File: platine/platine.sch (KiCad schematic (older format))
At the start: 16 parts

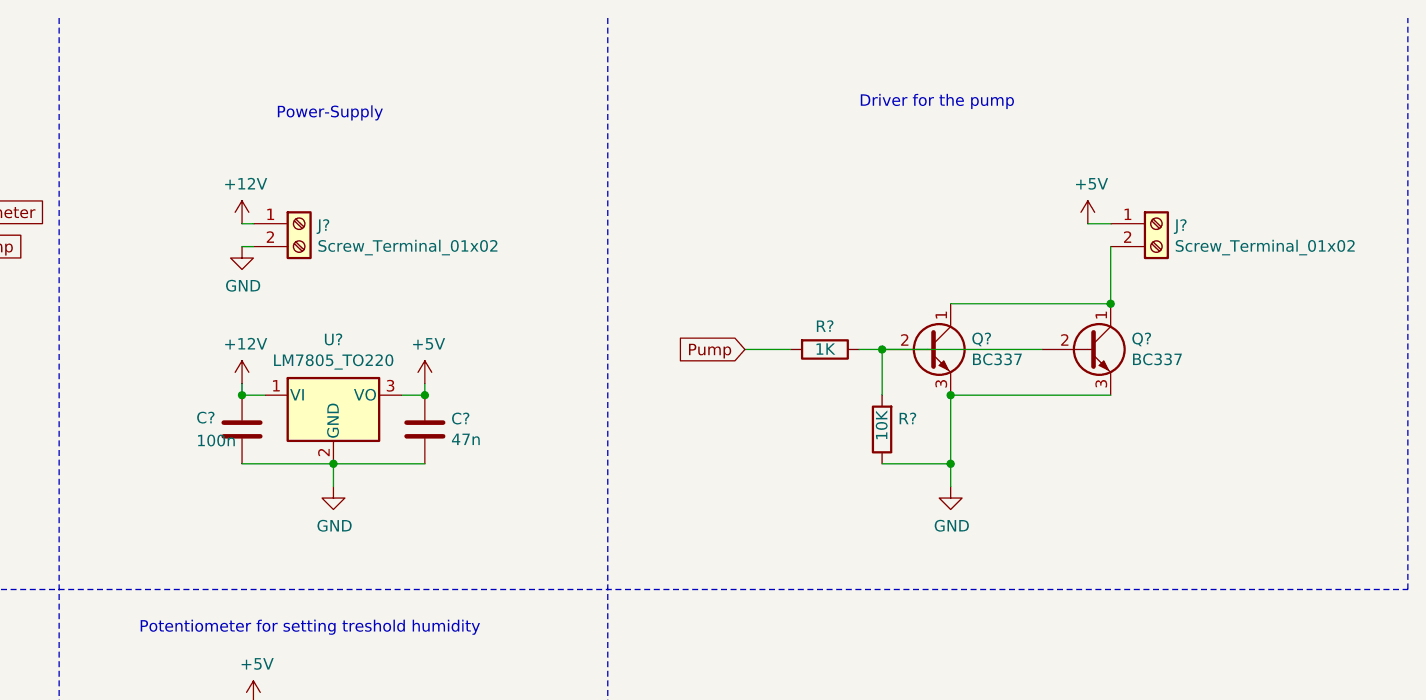
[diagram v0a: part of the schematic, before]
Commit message: Firmware timer-based and removed unnecessaries from scematics
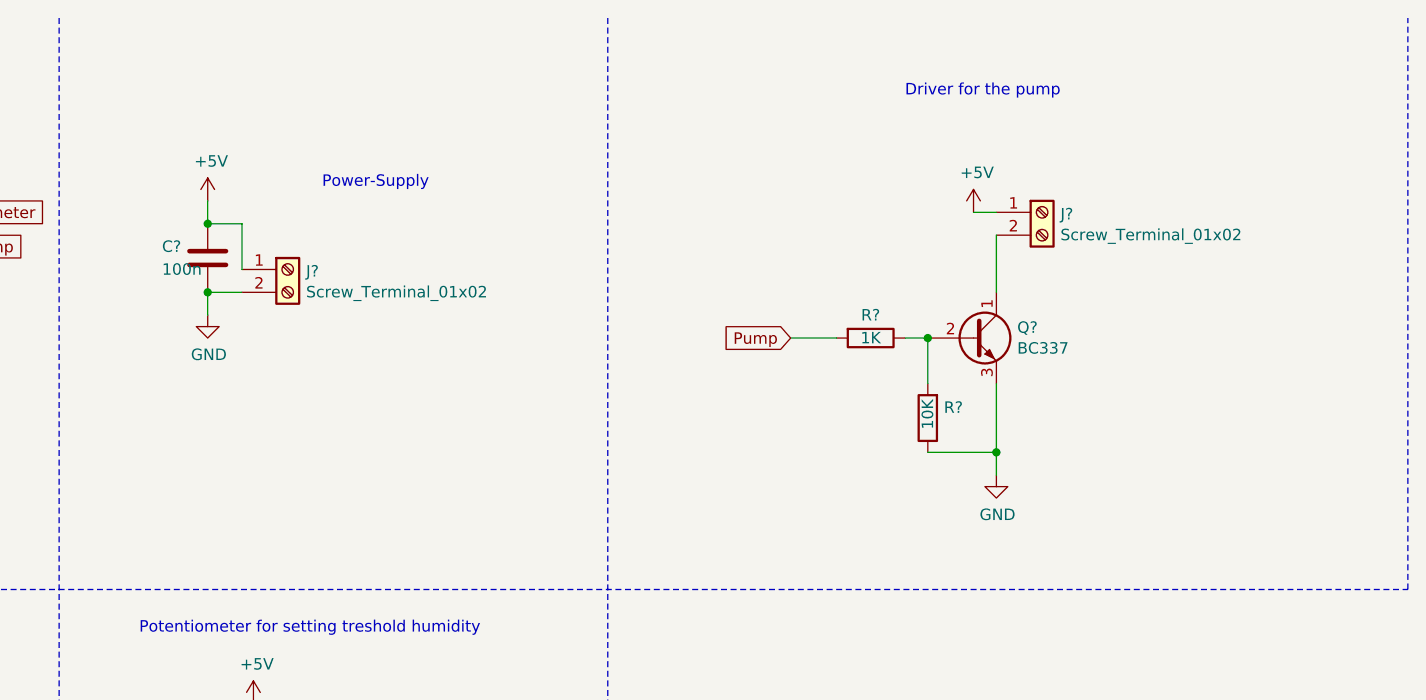
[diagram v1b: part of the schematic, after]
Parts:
- removed C?: 47n, symbol Device:C
- removed C?: 100n, symbol Device:C
- removed Q?: BC337, Package_TO_SOT_THT:TO-92_Inline, symbol Transistor_BJT:BC337
- removed U?: LM7805_TO220, Package_TO_SOT_THT:TO-220-3_Vertical, symbol Regulator_Linear:LM7805_TO220
- added C?: 100n, symbol Device:C
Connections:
- net +12V is gone; now on net +5V: J?.1 (Pin_1)
- net +5V: now also C?.1
- net GND: now also C?.2
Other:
- moved on the sheet: J?, Q?, R?

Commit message: scematics ready
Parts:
- removed J?: Conn_01x03_Male, symbol Connector:Conn_01x03_Male
- removed R?: 10K, symbol Device:R
- added D?: LED, symbol Device:LED
- added J?: Screw_Terminal_01x02, symbol Connector:Screw_Terminal_01x02
- added Q?: BC547, Package_TO_SOT_THT:TO-92_Inline, symbol Transistor_BJT:BC547
- added R? (x3): 220, symbol Device:R
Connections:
- net +5V: now also D?.2 (A), Q?.1 (C), R?.2
- net GND: now also R?.1
- net at J?.2 (Pin_2), Q?.1 (C): now also R?.1
- new net: J?.2 (Pin_2), Q?.2 (B)
- new net: J?.1 (Pin_1), R?.1
- new net: D?.1 (K), R?.2
- new net Sensor: Q?.3 (E), R?.2
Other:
- note added: "Sensor Connection"
- note added: "Sensor driver"
- note added: "To-Do:\n- Programmer-interface\n- alles zusammen verbinden"
- note removed: "To-Do:\n- Status-LED\n- Programmer-interface\n- Sensor nachbauen\n- alles zusammen verbinden"
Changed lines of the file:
@@
-$EndComp
-$Comp
-L Connector:Conn_01x03_Male J?
-U 1 1 6089F844
-P 4000 5250
-F 0 "J?" H 4108 5531 50  0000 C CNN
-F 1 "Conn_01x03_Male" H 4108 5440 50  0000 C CNN
-F 2 "" H 4000 5250 50  0001 C CNN
-F 3 "~" H 4000 5250 50  0001 C CNN
-	1    4000 5250
-	1    0    0    -1
 $EndComp
 $Comp
@@
 $Comp
 L Device:R R?
-U 1 1 608AA9A4
-P 7200 2250
-F 0 "R?" H 7130 2204 50  0000 R CNN
-F 1 "10K" V 7200 2300 50  0000 R CNN
-F 2 "" V 7130 2250 50  0001 C CNN
-F 3 "~" H 7200 2250 50  0001 C CNN
-	1    7200 2250
-	-1   0    0    1
-$EndComp
-Wire Wire Line
-	7200 2400 7500 2400
-Wire Wire Line
-	7500 2400 7500 2100
-Wire Wire Line
-	7200 2100 7200 1900
-Connection ~ 7200 1900
-$Comp
-L Device:R R?
 U 1 1 608B0CE2
 P 6950 1900
@@
 $EndComp
 Wire Wire Line
-	7500 1450 7500 1700
+	7500 1450 7500 1650
 $Comp
 L power:+5V #PWR?
@@
 Wire Wire Line
 	7400 1350 7500 1350
-$Comp
-L power:GND #PWR?
-U 1 1 608BD303
-P 7500 2500
-F 0 "#PWR?" H 7500 2250 50  0001 C CNN
-F 1 "GND" H 7505 2327 50  0000 C CNN
-F 2 "" H 7500 2500 50  0001 C CNN
-F 3 "" H 7500 2500 50  0001 C CNN
-	1    7500 2500
-	1    0    0    -1
-$EndComp
-Wire Wire Line
-	7500 2500 7500 2400
-Connection ~ 7500 2400
 $Comp
 L power:GND #PWR?
@@
 Wire Wire Line
 	6600 1900 6800 1900
-Wire Notes Line
-	9300 3000 9300 500
 Wire Notes Line
 	500  3000 9300 3000
@@
 	3400 500  3400 4500
 Text Notes 2150 5350 0    50   ~ 0
-To-Do:\n- Status-LED\n- Programmer-interface\n- Sensor nachbauen\n- alles zusammen verbinden
+To-Do:\n- Programmer-interface\n- alles zusammen verbinden
 $Comp
 L Device:R_POT RV?
@@
 Wire Notes Line
 	5800 500  5800 4500
-Wire Notes Line
-	500  4500 5800 4500
 Text Notes 3750 3200 0    50   ~ 0
 Potentiometer for setting treshold humidity
@@
 	4050 1300 4050 1400
 Connection ~ 4050 1400
+Wire Wire Line
+	7500 2100 7500 2500
+$Comp
+L Transistor_BJT:BC547 Q?
+U 1 1 608DC426
+P 7100 3850
+F 0 "Q?" V 7335 3850 50  0000 C CNN
+F 1 "BC547" V 7426 3850 50  0000 C CNN
+F 2 "Package_TO_SOT_THT:TO-92_Inline" H 7300 3775 50  0001 L CIN
+F 3 "https://www.onsemi.com/pub/Collateral/BC550-D.pdf" H 7100 3850 50  0001 L CNN
+	1    7100 3850
+	0    -1   1    0
+$EndComp
+$Comp
+L Connector:Screw_Terminal_01x02 J?
+U 1 1 608DCD99
+P 7500 3450
+F 0 "J?" H 7580 3442 50  0000 L CNN
+F 1 "Screw_Terminal_01x02" H 7580 3351 50  0000 L CNN
+F 2 "" H 7500 3450 50  0001 C CNN
+F 3 "~" H 7500 3450 50  0001 C CNN
+	1    7500 3450
+	1    0    0    -1
+$EndComp
+$Comp
+L Device:R R?
+U 1 1 608DD3E9
+P 7000 3450
+F 0 "R?" V 6900 3450 50  0000 C CNN
+F 1 "220" V 7000 3450 50  0000 C CNN
+F 2 "" V 6930 3450 50  0001 C CNN
+F 3 "~" H 7000 3450 50  0001 C CNN
+	1    7000 3450
+	0    1    1    0
+$EndComp
+Wire Wire Line
+	7150 3450 7300 3450
+Wire Wire Line
+	7100 3650 7100 3550
+Wire Wire Line
+	7100 3550 7300 3550
+$Comp
+L power:+5V #PWR?
+U 1 1 608E30DE
+P 6500 3950
+F 0 "#PWR?" H 6500 3800 50  0001 C CNN
+F 1 "+5V" H 6515 4123 50  0000 C CNN
+F 2 "" H 6500 3950 50  0001 C CNN
+F 3 "" H 6500 3950 50  0001 C CNN
+	1    6500 3950
+	1    0    0    -1
+$EndComp
+Wire Wire Line
+	6850 3450 6850 3950
+Wire Wire Line
+	6850 3950 6500 3950
+Wire Wire Line
+	6850 3950 6900 3950
+Connection ~ 6850 3950
+$Comp
+L Device:R R?
+U 1 1 608E5A48
+P 7650 3950
+F 0 "R?" V 7550 3950 50  0000 C CNN
+F 1 "220" V 7650 3950 50  0000 C CNN
+F 2 "" V 7580 3950 50  0001 C CNN
+F 3 "~" H 7650 3950 50  0001 C CNN
+	1    7650 3950
+	0    1    1    0
+$EndComp
+Wire Wire Line
+	7300 3950 7400 3950
+$Comp
+L power:GND #PWR?
+U 1 1 608BD303
+P 7500 2500
+F 0 "#PWR?" H 7500 2250 50  0001 C CNN
+F 1 "GND" H 7505 2327 50  0000 C CNN
+F 2 "" H 7500 2500 50  0001 C CNN
+F 3 "" H 7500 2500 50  0001 C CNN
+	1    7500 2500
+	1    0    0    -1
+$EndComp
+$Comp
+L power:GND #PWR?
+U 1 1 608E6C80
+P 8050 3950
+F 0 "#PWR?" H 8050 3700 50  0001 C CNN
+F 1 "GND" H 8055 3777 50  0000 C CNN
+F 2 "" H 8050 3950 50  0001 C CNN
+F 3 "" H 8050 3950 50  0001 C CNN
+	1    8050 3950
+	1    0    0    -1
+$EndComp
+Wire Wire Line
+	8050 3950 7800 3950
+Text Notes 7700 3500 0    50   ~ 0
+Sensor Connection
+Text GLabel 7500 4250 2    50   Input ~ 0
+Sensor
+Wire Wire Line
+	7500 4250 7400 4250
+Wire Wire Line
+	7400 4250 7400 3950
+Connection ~ 7400 3950
+Wire Wire Line
+	7400 3950 7500 3950
+Text GLabel 2950 1700 2    50   Input ~ 0
+Sensor
+Wire Notes Line
+	9300 500  9300 4500
+Text Notes 7150 3250 0    50   ~ 0
+Sensor driver
+$Comp
+L Device:R R?
+U 1 1 608EEB47
+P 7200 1650
+F 0 "R?" V 7100 1650 50  0000 C CNN
+F 1 "220" V 7200 1650 50  0000 C CNN
+F 2 "" V 7130 1650 50  0001 C CNN
+F 3 "~" H 7200 1650 50  0001 C CNN
+	1    7200 1650
+	0    1    1    0
+$EndComp
+$Comp
+L Device:LED D?
+U 1 1 608ED5E0
+P 6900 1500
+F 0 "D?" V 6900 1600 50  0000 L CNN
+F 1 "LED" V 7000 1600 50  0000 L CNN
+F 2 "" H 6900 1500 50  0001 C CNN
+F 3 "~" H 6900 1500 50  0001 C CNN
+	1    6900 1500
+	0    -1   -1   0
+$EndComp
+Wire Wire Line
+	6900 1350 7400 1350
+Connection ~ 7400 1350
+Wire Wire Line
+	6900 1650 7050 1650
+Wire Wire Line
+	7350 1650 7500 1650
+Connection ~ 7500 1650
+Wire Wire Line
+	7500 1650 7500 1700
+Wire Notes Line
+	500  4500 9300 4500
 $EndSCHEMATC

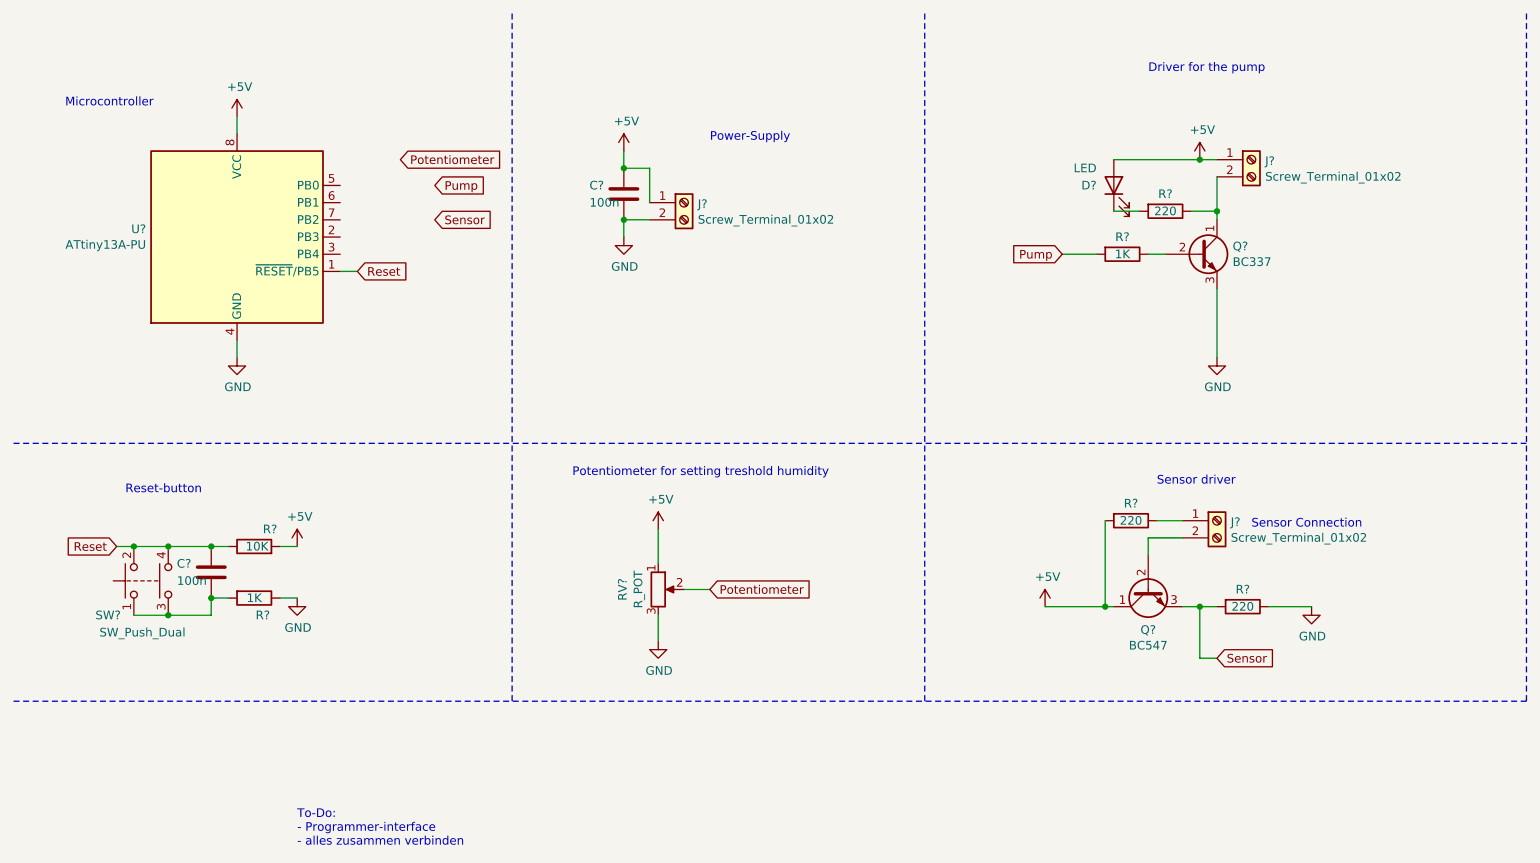
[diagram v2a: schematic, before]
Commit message: pcb footprints assigned
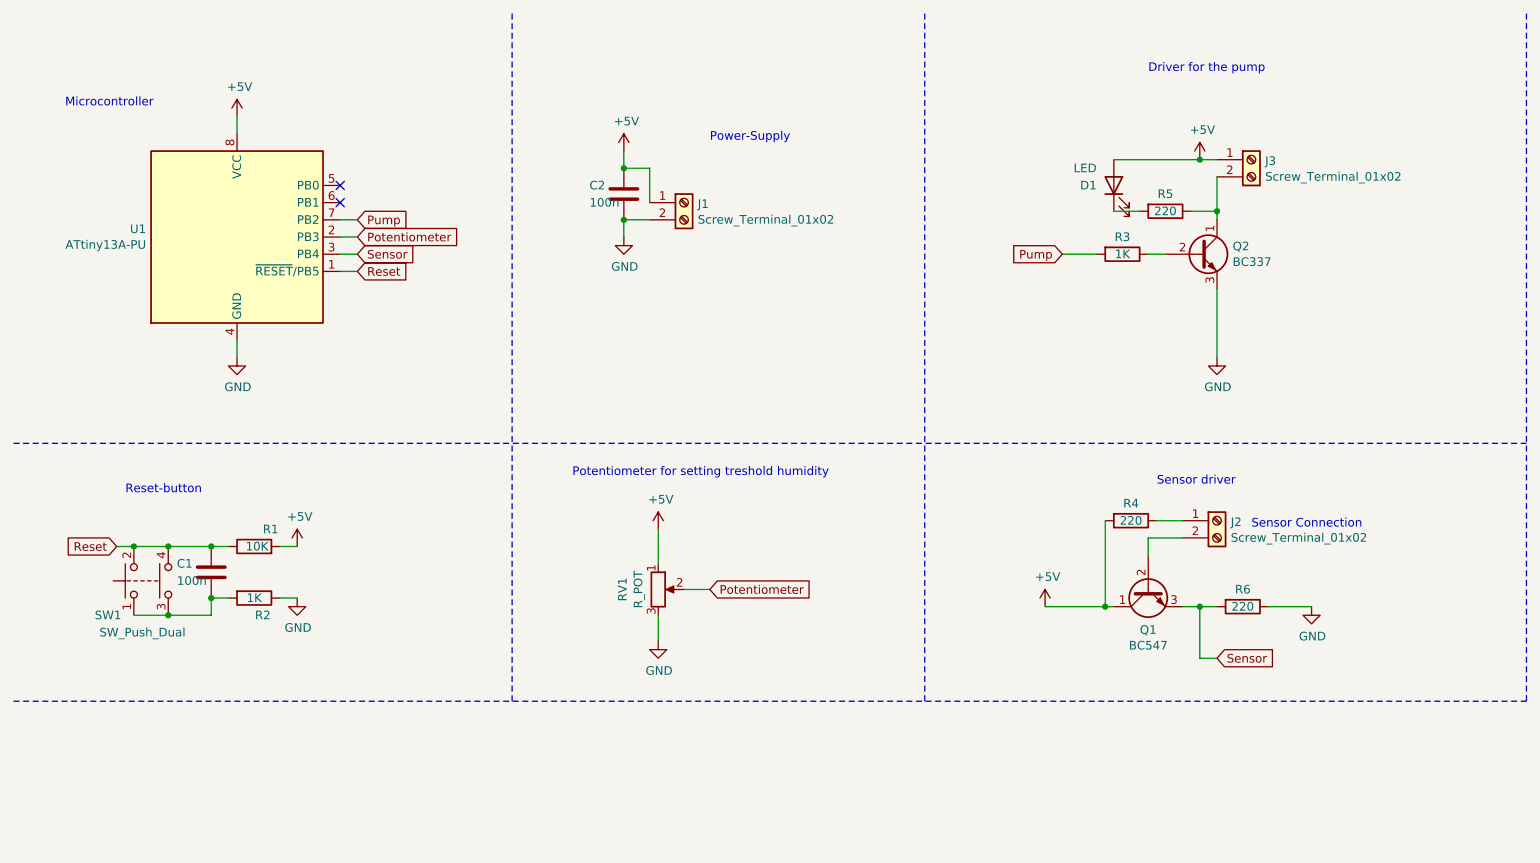
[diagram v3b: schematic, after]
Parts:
- C1, C2: renamed from C?; footprint (none) -> Capacitor_THT:C_Disc_D6.0mm_W2.5mm_P5.00mm
- D1: renamed from D?; footprint (none) -> LED_THT:LED_D5.0mm
- J1, J2, J3: renamed from J?; footprint (none) -> TerminalBlock_Phoenix:TerminalBlock_Phoenix_MKDS-1,5-2-5.08_1x02_P5.08mm_Horizontal
- R1, R2, R3, R4, R5, R6: renamed from R?; footprint (none) -> Resistor_THT:R_Axial_DIN0207_L6.3mm_D2.5mm_P7.62mm_Horizontal
- RV1: renamed from RV?; footprint (none) -> Potentiometer_THT:Potentiometer_Alps_RK163_Single_Horizontal
- SW1: renamed from SW?; footprint (none) -> Button_Switch_THT:SW_TH_Tactile_Omron_B3F-10xx
- gave numbers to parts that had none: 3
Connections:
- net Potentiometer: now also U1.2 (PB3)
- net Pump: now also U1.7 (PB2)
- net Sensor: now also U1.3 (PB4)
- no-connect marks 0 -> 2
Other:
- note removed: "To-Do:\n- Programmer-interface\n- alles zusammen verbinden"

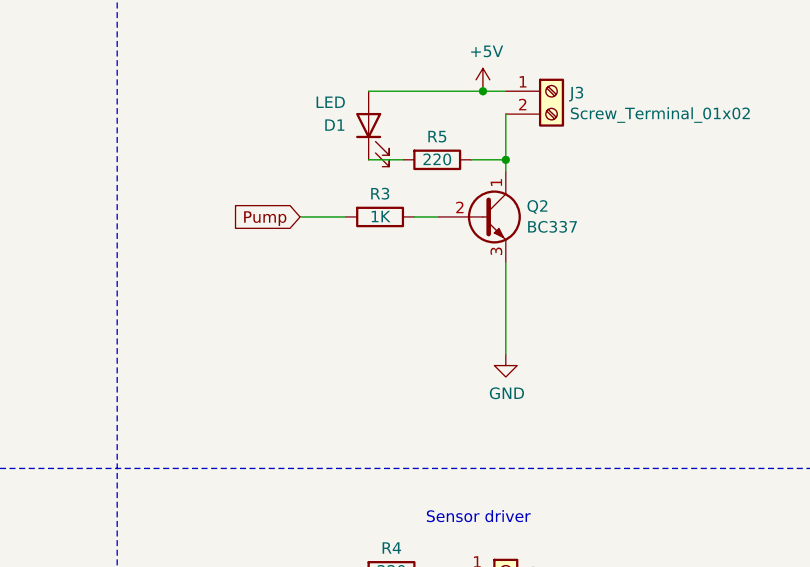
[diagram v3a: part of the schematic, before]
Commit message: PCB: Added capacitor to smooth signal
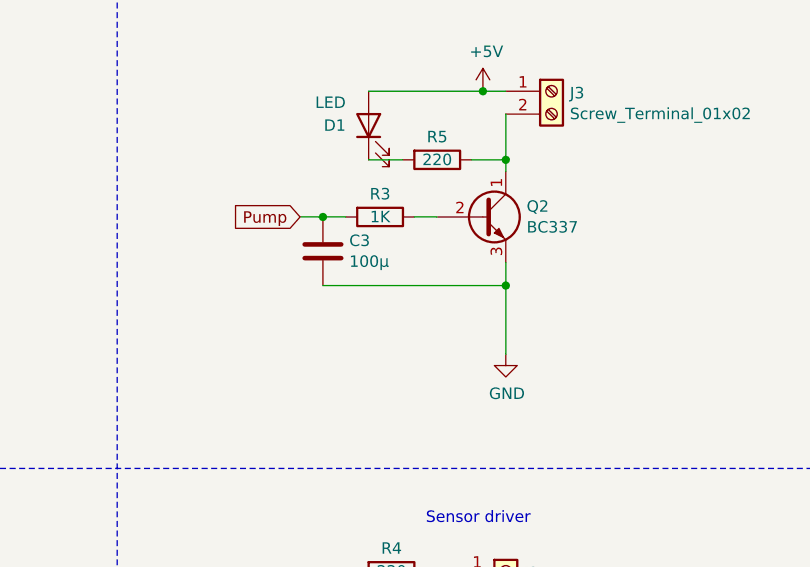
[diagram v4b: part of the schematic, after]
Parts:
- added C3: 100µ, Capacitor_THT:CP_Radial_D5.0mm_P2.50mm, symbol Device:C
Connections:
- net GND: now also C3.2
- net Pump: now also C3.1
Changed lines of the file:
@@
 Pump
 Wire Wire Line
-	6600 1900 6800 1900
+	6600 1900 6700 1900
 Wire Notes Line
 	500  3000 9300 3000
@@
 Connection ~ 4050 1400
 Wire Wire Line
-	7500 2100 7500 2500
+	7500 2100 7500 2200
 $Comp
 L Transistor_BJT:BC547 Q1
@@
 NoConn ~ 2400 1500
 NoConn ~ 2400 1600
+$Comp
+L Device:C C3
+U 1 1 6093544D
+P 6700 2050
+F 0 "C3" H 6815 2096 50  0000 L CNN
+F 1 "100µ" H 6815 2005 50  0000 L CNN
+F 2 "Capacitor_THT:CP_Radial_D5.0mm_P2.50mm" H 6738 1900 50  0001 C CNN
+F 3 "~" H 6700 2050 50  0001 C CNN
+	1    6700 2050
+	1    0    0    -1
+$EndComp
+Connection ~ 6700 1900
+Wire Wire Line
+	6700 1900 6800 1900
+Wire Wire Line
+	6700 2200 7500 2200
+Connection ~ 7500 2200
+Wire Wire Line
+	7500 2200 7500 2500
 $EndSCHEMATC
